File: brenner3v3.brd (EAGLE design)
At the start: 100 x 80 mm, 14 parts, among them IC1 REG1117, Q2 BC328, Q3 BC328

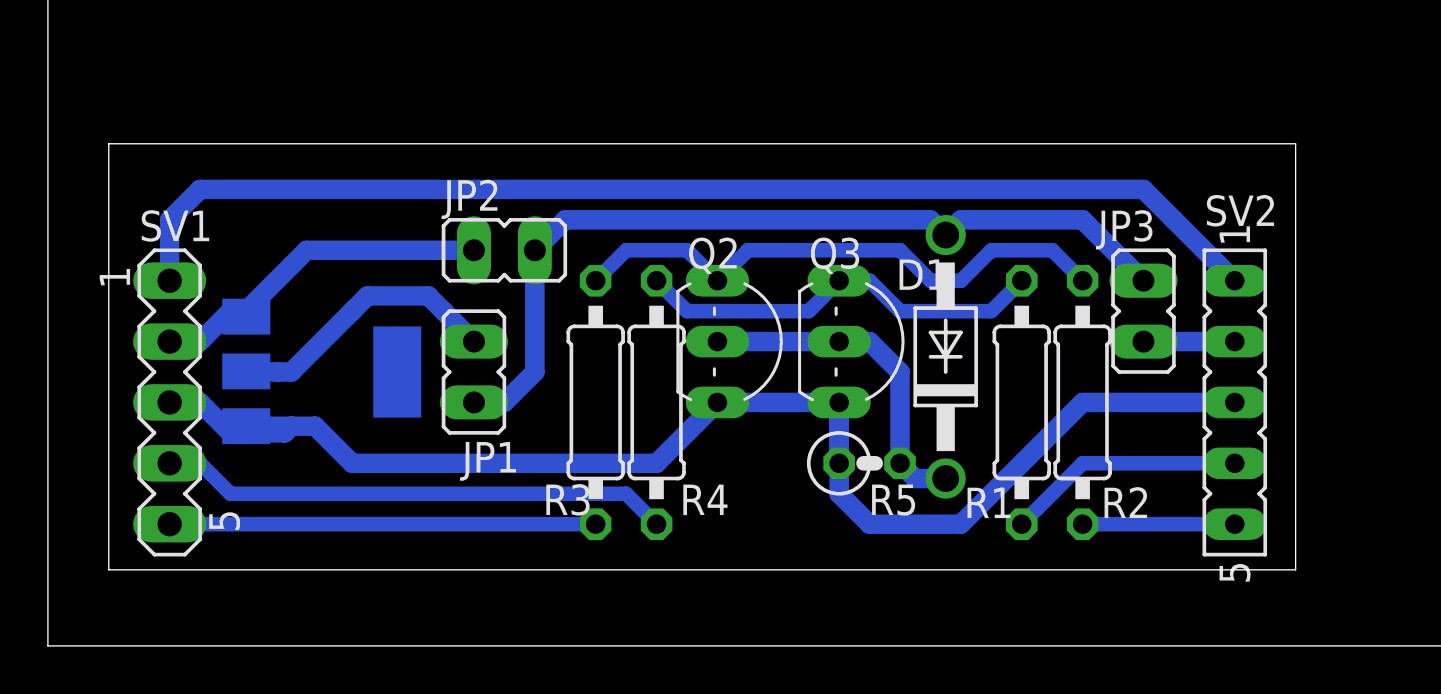
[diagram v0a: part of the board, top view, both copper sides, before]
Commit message: Simplified schematic & layout
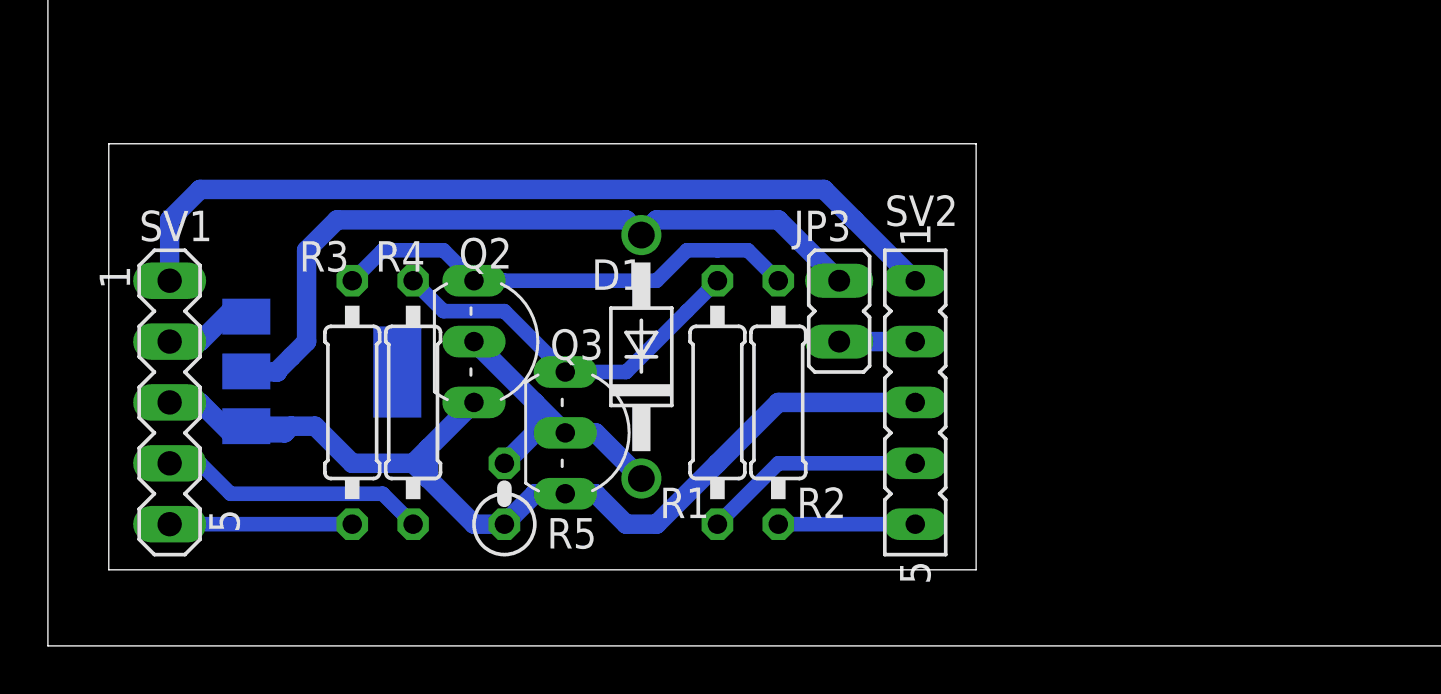
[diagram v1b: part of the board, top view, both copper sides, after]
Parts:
- removed JP1, JP2: (no value), jumper:JP1
- moved R5 15.3 mm to (19.1, 6.35), turned to 90 degrees
- moved SV2 13.3 mm to (36.2, 10.2)
- moved D1 12.7 mm to (24.8, 12.1)
- moved R1 12.7 mm to (27.9, 10.2)
- moved R2 12.7 mm to (30.5, 10.2)
- moved JP3 12.7 mm to (33.0, 14.0)
- moved Q3 12.0 mm to (22.9, 8.89)
- moved Q2 10.2 mm to (19.1, 12.7)
- moved R3 10.2 mm to (12.7, 10.2)
- moved R4 10.2 mm to (15.2, 10.2)
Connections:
- removed net N$1: IC1.2, JP1.2
- net N$12: now also IC1.2; no longer JP1.1, JP2.2
- net VDD5V: no longer JP2.1
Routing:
- net VSS: track 57.6 -> 43.3 mm
- net VPP: track 49.1 -> 35.8 mm
- net N$1: track 11.6 -> 0.00 mm
- net VDD5V: track 14.6 -> 3.82 mm
- net N$5: track 17.8 -> 7.62 mm
- net N$4: track 21.4 -> 11.2 mm
- net N$12: track 35.7 -> 31.3 mm
- net N$7: track 23.5 -> 19.9 mm
- net N$6: track 17.3 -> 15.9 mm
- net VDD3V3: track 3.81 -> 3.17 mm
- net N$9: track 6.35 -> 5.71 mm
- net N$8: track 9.94 -> 9.31 mm
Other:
- outline, holes or cut-outs redrawn
